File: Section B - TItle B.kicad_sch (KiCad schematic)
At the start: 25 parts, among them J14 JST_SHBM04B-SRSS-TB, J2 Conn_02x07_Odd_Even, J7 Micro_SD_Card_Det, J8 THD-20-R, J9 THD-02-R, SW1 Right angle Tact button, U1 TPD4EUSB30, U18 RT9742GGJ5, U2 TPD4EUSB30, U3 MagJack-A70-112-331N126, U5 74LVC1G07SE-7

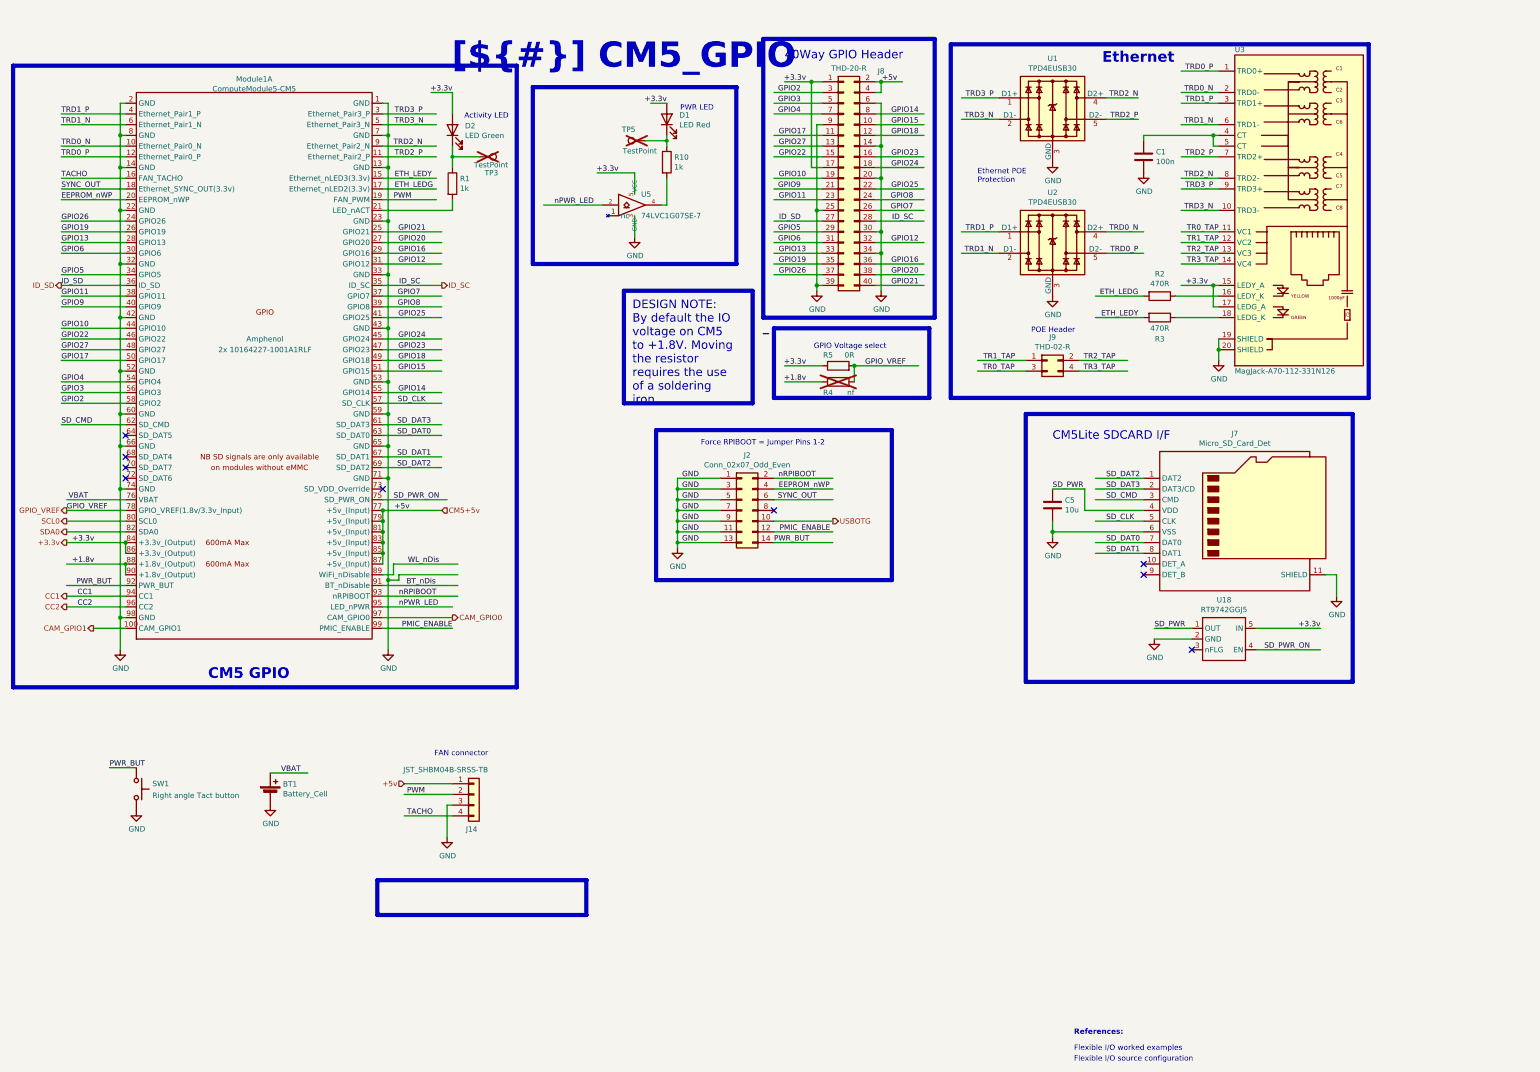
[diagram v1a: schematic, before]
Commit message: Progress in power input and sata power option
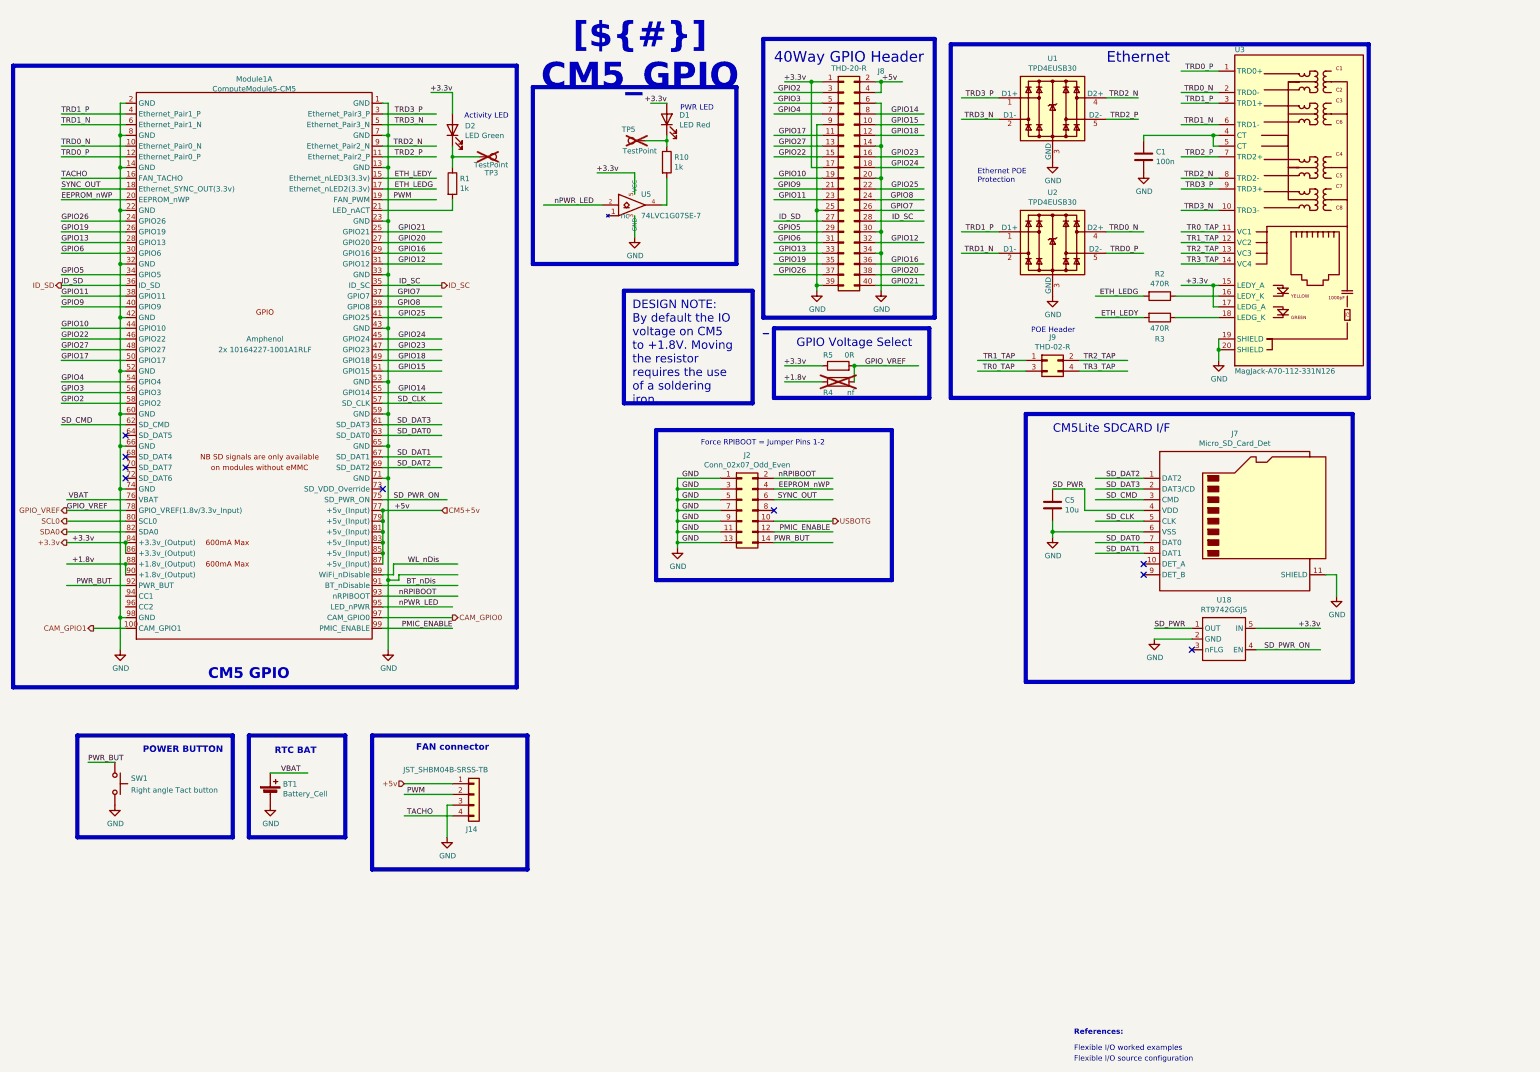
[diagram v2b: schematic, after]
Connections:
- net CC1: no longer names the net of Module1.94 (CC1)
- net CC2: no longer names the net of Module1.96 (CC2)
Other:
- note added: "POWER BUTTON"
- note added: "RTC BAT"
- note removed: "40Way GPIO Header"
- note removed: "CM5Lite SDCARD I/F"
- note removed: "GPIO Voltage select"
- moved on the sheet: SW1
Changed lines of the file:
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@@
 	)
 	(rectangle
+		(start 29.21 179.07)
+		(end 66.04 203.2)
+		(stroke
+			(width 1)
+			(type default)
+			(color 200 200 200 1)
+		)
+		(fill
+			(type none)
+		)
+	)
+	(rectangle
 		(start 166.37 106.68)
 		(end 222.25 142.24)
@@
 	)
 	(rectangle
-		(start 100.33 213.36)
-		(end 149.86 221.615)
+		(start 69.85 179.07)
+		(end 92.71 203.2)
+		(stroke
+			(width 1)
+			(type default)
+			(color 200 200 200 1)
+		)
+		(fill
+			(type none)
+		)
+	)
+	(rectangle
+		(start 99.06 179.07)
+		(end 135.89 210.82)
 		(stroke
 			(width 1)
@@
 		(effects
 			(font
+				(face "Times New Roman")
 				(size 1.27 1.27)
 				(color 162 22 34 1)
@@
 		)
 	)
-	(text "CM5Lite SDCARD I/F"
+	(text "POWER BUTTON"
 		(exclude_from_sim no)
-		(at 260.35 109.22 0)
+		(at 44.704 183.388 0)
 		(effects
 			(font
-				(size 2.007 2.007)
+				(face "Times New Roman")
+				(size 1.524 1.524)
+				(bold yes)
 				(color 162 22 34 1)
 			)
@@
 		)
 	)
-	(text "GPIO Voltage select\n"
-		(exclude_from_sim no)
-		(at 220.98 87.63 0)
-		(effects
-			(font
-				(size 1.27 1.27)
-				(color 162 22 34 1)
-			)
-			(justify right bottom)
-		)
-	)
 	(text "Ethernet POE\nProtection"
 		(exclude_from_sim no)
@@
 		)
 	)
-	(text "40Way GPIO Header"
-		(exclude_from_sim no)
-		(at 196.85 19.05 0)
-		(effects
-			(font
-				(size 2.007 2.007)
-				(color 162 22 34 1)
-			)
-			(justify left bottom)
-		)
-	)
 	(text "FAN connector\n"
 		(exclude_from_sim no)
-		(at 113.792 184.15 0)
+		(at 109.474 182.88 0)
 		(effects
 			(font
-				(size 1.27 1.27)
+				(face "Times New Roman")
+				(size 1.524 1.524)
+				(bold yes)
 				(color 162 22 34 1)
 			)
@@
 		)
 	)
+	(text "RTC BAT"
+		(exclude_from_sim no)
+		(at 75.946 183.642 0)
+		(effects
+			(font
+				(face "Times New Roman")
+				(size 1.524 1.524)
+				(bold yes)
+				(color 162 22 34 1)
+			)
+			(justify left bottom)
+		)
+	)
 	(text "Flexible I/O source configuration"
 		(exclude_from_sim no)
@@
 		)
 	)
+	(text_box "GPIO Voltage Select"
+		(exclude_from_sim no)
+		(at 129.54 79.375 0)
+		(size 167.64 9.525)
+		(margins 1.9049 1.9049 1.9049 1.9049)
+		(stroke
+			(width -0.0001)
+			(type solid)
+		)
+		(fill
+			(type none)
+		)
+		(effects
+			(font
+				(face "Times New Roman")
+				(size 2 2)
+				(thickness 0.3175)
+				(color 162 22 34 1)
+			)
+			(justify bottom)
+		)
+	)
+	(text_box "CM5Lite SDCARD I/F"
+		(exclude_from_sim no)
+		(at 254 99.695 0)
+		(size 40.64 9.525)
+		(margins 1.9049 1.9049 1.9049 1.9049)
+		(stroke
+			(width -0.0001)
+			(type solid)
+		)
+		(fill
+			(type none)
+		)
+		(effects
+			(font
+				(face "Times New Roman")
+				(size 2 2)
+				(thickness 0.3175)
+				(color 162 22 34 1)
+			)
+			(justify bottom)
+		)
+	)
 	(text_box "CM5 GPIO"
 		(exclude_from_sim no)
@@
 		)
 	)
+	(text_box "40Way GPIO Header"
+		(exclude_from_sim no)
+		(at 190.5 12.065 0)
+		(size 43.18 9.525)
+		(margins 1.9049 1.9049 1.9049 1.9049)
+		(stroke
+			(width -0.0001)
+			(type solid)
+		)
+		(fill
+			(type none)
+		)
+		(effects
+			(font
+				(face "Times New Roman")
+				(size 2.54 2.54)
+				(thickness 0.3175)
+				(color 162 22 34 1)
+			)
+			(justify bottom)
+		)
+	)
 	(text_box "[${#}] ${TITLE}"
 		(exclude_from_sim no)
-		(at 110.49 11.43 0)
-		(size 96.52 12.7)
+		(at 127 11.43 0)
+		(size 71.12 12.7)
 		(margins 5.9999 5.9999 5.9999 5.9999)
 		(stroke
@@
 				(face "Times New Roman")
 				(size 2.54 2.54)
-				(thickness 0.508)
-				(bold yes)
+				(thickness 0.3175)
 				(color 162 22 34 1)
 			)
@@
 	(wire
 		(pts
-			(xy 36.83 186.69) (xy 43.18 186.69)
+			(xy 31.75 185.42) (xy 38.1 185.42)
 		)
 		(stroke
@@
 	(wire
 		(pts
-			(xy 26.67 148.59) (xy 40.64 148.59)
-		)
-		(stroke
-			(width 0)
-			(type solid)
-		)
-	)
-	(wire
-		(pts
 			(xy 39.37 54.61) (xy 39.37 67.31)
 		)
@@
 	(wire
 		(pts
-			(xy 26.67 146.05) (xy 40.64 146.05)
-		)
-		(stroke
-			(width 0)
-			(type solid)
-		)
-	)
-	(wire
-		(pts
 			(xy 102.87 44.45) (xy 102.87 57.15)
 		)
@@
 		)
 	)
-	(label "CC2"
-		(at 29.21 148.59 0)
-		(effects
-			(font
-				(size 1.27 1.27)
-			)
-			(justify left bottom)
-		)
-	)
 	(label "GPIO25"
 		(at 228.6 49.53 180)
@@
 		)
 	)
-	(label "CC1"
-		(at 29.21 146.05 0)
-		(effects
-			(font
-				(size 1.27 1.27)
-			)
-			(justify left bottom)
-		)
-	)
 	(label "GPIO15"
 		(at 228.6 34.29 180)
@@
 	)
 	(label "PWR_BUT"
-		(at 36.83 186.69 0)
+		(at 31.75 185.42 0)
 		(effects
 			(font
@@
 		)
 	)
-	(hierarchical_label "CC2"
-		(shape output)
-		(at 26.67 148.59 180)
-		(effects
-			(font
-				(size 1.27 1.27)
-			)
-			(justify right)
-		)
-	)
 	(hierarchical_label "ID_SD"
 		(shape output)
@@
 		)
 	)
-	(hierarchical_label "CC1"
-		(shape output)
-		(at 26.67 146.05 180)
-		(effects
-			(font
-				(size 1.27 1.27)
-			)
-			(justify right)
-		)
-	)
 	(hierarchical_label "SDA0"
 		(shape output)
@@
 	(symbol
 		(lib_id "Switch:SW_Push")
-		(at 43.18 191.77 270)
+		(at 38.1 190.5 270)
 		(unit 1)
 		(exclude_from_sim no)
@@
 		(dnp no)
 		(property "Reference" "SW1"
-			(at 46.99 190.4999 90)
+			(at 41.91 189.2299 90)
 			(effects
 				(font
@@
 		)
 		(property "Value" "Right angle Tact button"
-			(at 46.99 193.294 90)
+			(at 41.91 192.024 90)
 			(effects
 				(font
@@
 		)
 		(property "Footprint" "Button_Switch_THT:SW_Tactile_SPST_Angled_PTS645Vx58-2LFS"
-			(at 48.26 191.77 0)
+			(at 43.18 190.5 0)
 			(effects
 				(font
@@
 		)
 		(property "Datasheet" "https://www.mouser.co.uk/datasheet/2/240/Littelfuse-3050591.pdf"
-			(at 48.26 191.77 0)
+			(at 43.18 190.5 0)
 			(effects
 				(font
@@
 		)
 		(property "Description" "Push button switch, generic, two pins"
-			(at 43.18 191.77 0)
+			(at 38.1 190.5 0)
 			(effects
 				(font
@@
 		)
 		(property "Field5" "PTS645VH58-2LFS"
-			(at 43.18 191.77 0)
+			(at 38.1 190.5 0)
 			(effects
 				(font
@@
 		)
 		(property "Field6" "PTS645VH58-2LFS"
-			(at 43.18 191.77 0)
+			(at 38.1 190.5 0)
 			(effects
 				(font
@@
 		)
 		(property "Field7" "CK"
-			(at 43.18 191.77 0)
+			(at 38.1 190.5 0)
 			(effects
 				(font
@@
 		)
 		(property "Part Description" "Right angle through hole Tact switch"
-			(at 43.18 191.77 0)
+			(at 38.1 190.5 0)
 			(effects
 				(font
@@
 	(symbol
 		(lib_id "power:GND")
-		(at 43.18 196.85 0)
+		(at 38.1 195.58 0)
 		(unit 1)
 		(exclude_from_sim no)
@@
 		(dnp no)
 		(property "Reference" "#PWR030"
-			(at 43.18 203.2 0)
+			(at 38.1 201.93 0)
 			(effects
 				(font
@@
 		)
 		(property "Value" "GND"
-			(at 43.307 201.2442 0)
+			(at 38.227 199.9742 0)
 			(effects
 				(font
@@
 		)
 		(property "Footprint" ""
-			(at 43.18 196.85 0)
+			(at 38.1 195.58 0)
 			(effects
 				(font
@@
 		)
 		(property "Datasheet" ""
-			(at 43.18 196.85 0)
+			(at 38.1 195.58 0)
 			(effects
 				(font
@@
 		)
 		(property "Description" "Power symbol creates a global label with name \"GND\" , ground"
-			(at 43.18 196.85 0)
+			(at 38.1 195.58 0)
 			(effects
 				(font

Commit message: Voltage calcs
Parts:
- renumbered C5 to C19, C1 to C20, D2 to D3, D1 to D4, J8 to J10, J9 to J11, J7 to J12, J14 to J8, J2 to J9, R1 to R3, R10 to R4, R4 to R6, R2 to R7, R3 to R8, TP3 to TP1, TP5 to TP2, U5 to U2, U1 to U3, U2 to U4, U18 to U5, U3 to U6

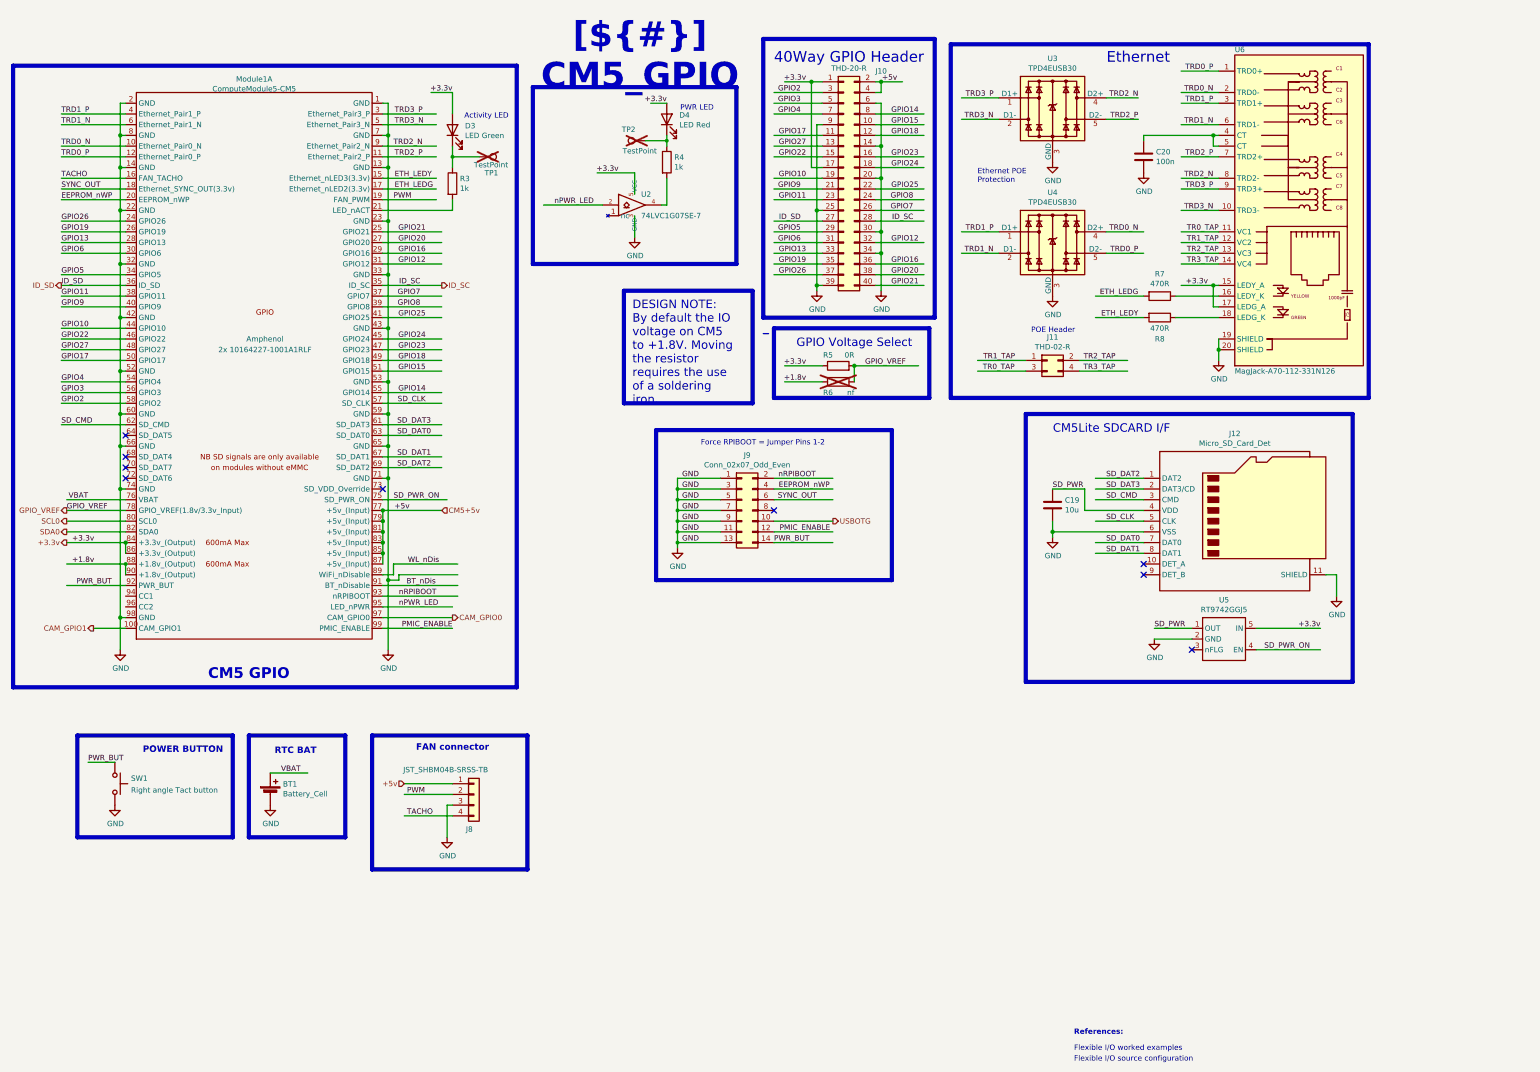
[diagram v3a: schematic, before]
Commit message: Sheet name edit and changed to net labels
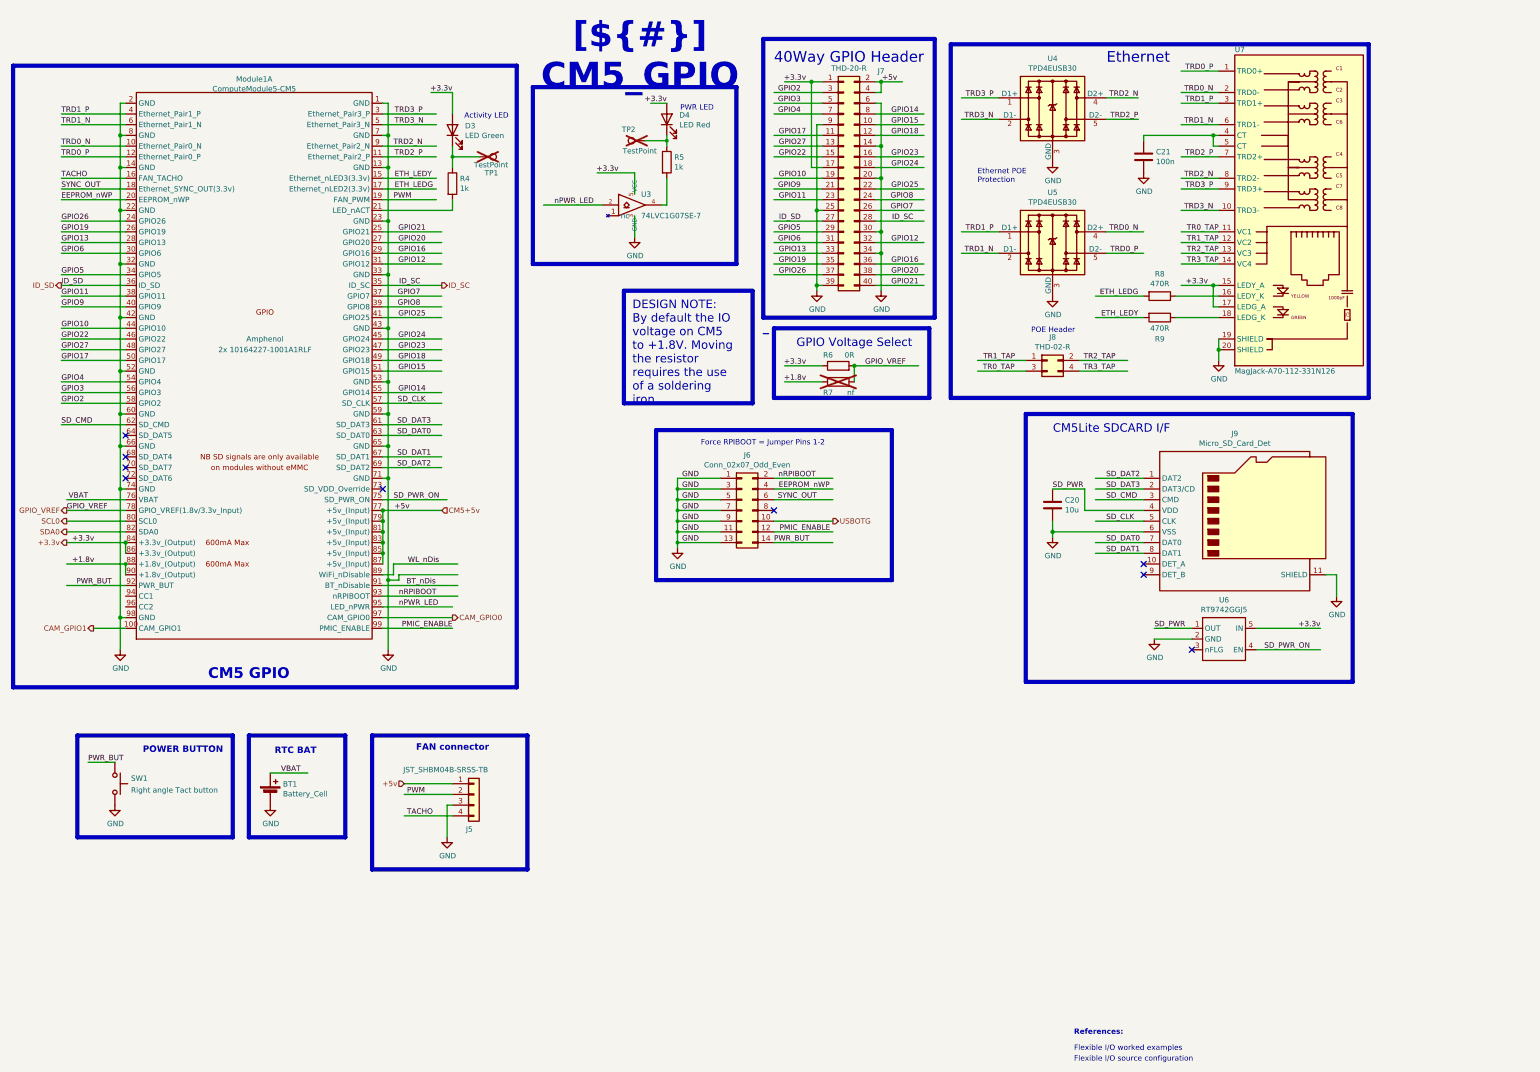
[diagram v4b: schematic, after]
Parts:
- renumbered C19 to C20, C20 to C21, J8 to J5, J9 to J6, J10 to J7, J11 to J8, J12 to J9, R3 to R4, R4 to R5, R5 to R6, R6 to R7, R7 to R8, R8 to R9, U2 to U3, U3 to U4, U4 to U5, U5 to U6, U6 to U7
